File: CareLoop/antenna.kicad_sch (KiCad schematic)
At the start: 5 parts, among them J1 Conn_Coaxial_Small

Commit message: updated antenna version
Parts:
- removed C30: C_Small, Capacitor_SMD:C_0603_1608Metric_Pad1.08x0.95mm_HandSolder, symbol Device:C_Small
- added L3: L_Small, symbol Device:L_Small
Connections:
- net GND: now also L3.2; no longer C29.2
- net at C20.2, C29.1: now also L3.1; no longer AE1.1 (FEED)
- new net: AE1.1 (FEED), C29.2
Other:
- moved on the sheet: C20

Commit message: updated antenna version
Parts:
- removed C29: C_Small, Capacitor_SMD:C_0603_1608Metric_Pad1.08x0.95mm_HandSolder, symbol Device:C_Small
- added L4: L_Small, symbol Device:L_Small
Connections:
- net at AE1.1 (FEED): now also L4.2
- net at C20.2, L3.1: now also L4.1
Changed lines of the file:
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@@
+	(symbol
+		(lib_id "Device:L_Small")
+		(at 124.46 93.98 90)
+		(unit 1)
+		(exclude_from_sim no)
+		(in_bom yes)
+		(on_board yes)
+		(dnp no)
+		(fields_autoplaced yes)
+		(property "Reference" "L4"
+			(at 124.46 88.9 90)
+			(effects
+				(font
+					(size 1.27 1.27)
+				)
+			)
+		)
+		(property "Value" "L_Small"
+			(at 124.46 91.44 90)
+			(effects
+				(font
+					(size 1.27 1.27)
+				)
+			)
+		)
+		(property "Footprint" ""
+			(at 124.46 93.98 0)
+			(effects
+				(font
+					(size 1.27 1.27)
+				)
+				(hide yes)
+			)
+		)
+		(property "Datasheet" "~"
+			(at 124.46 93.98 0)
+			(effects
+				(font
+					(size 1.27 1.27)
+				)
+				(hide yes)
+			)
+		)
+		(property "Description" "Inductor, small symbol"
+			(at 124.46 93.98 0)
+			(effects
+				(font
+					(size 1.27 1.27)
+				)
+				(hide yes)
+			)
+		)
+		(pin "1"
+		)
+		(pin "2"
+		)
+		(instances
+			(project "CareLoop_PCB"
+				(path "/1249f778-de2d-49b4-b768-08b76b87278f/6a4240b2-fe07-4b72-99e3-52c15e65d120"
+					(reference "L4")
+					(unit 1)
+				)
+			)
+		)
+	)
 	(symbol
 		(lib_id "Device:L_Small")
@@
 					(unit 1)
 				)
-			)
-		)
-	)
-	(symbol
-		(lib_id "Device:C_Small")
-		(at 124.46 93.98 90)
-		(unit 1)
-		(exclude_from_sim no)
-		(in_bom yes)
-		(on_board yes)
-		(dnp no)
-		(fields_autoplaced yes)
-		(property "Reference" "C29"
-			(at 124.4663 87.63 90)
-			(effects
-				(font
-					(size 1.27 1.27)
-				)
-			)
-		)
-		(property "Value" "C_Small"
-			(at 124.4663 90.17 90)
-			(effects
-				(font
-					(size 1.27 1.27)
-				)
-			)
-		)
-		(property "Footprint" "Capacitor_SMD:C_0603_1608Metric_Pad1.08x0.95mm_HandSolder"
-			(at 124.46 93.98 0)
-			(effects
-				(font
-					(size 1.27 1.27)
-				)
-				(hide yes)
-			)
-		)
-		(property "Datasheet" "~"
-			(at 124.46 93.98 0)
-			(effects
-				(font
-					(size 1.27 1.27)
-				)
-				(hide yes)
-			)
-		)
-		(property "Description" "Unpolarized capacitor, small symbol"
-			(at 124.46 93.98 0)
-			(effects
-				(font
-					(size 1.27 1.27)
-				)
-				(hide yes)
-			)
-		)
-		(pin "2"
-		)
-		(pin "1"
-		)
-		(instances
-			(project "CareLoop_PCB"
-				(path "/1249f778-de2d-49b4-b768-08b76b87278f/6a4240b2-fe07-4b72-99e3-52c15e65d120"
-					(reference "C29")
-					(unit 1)
-				)

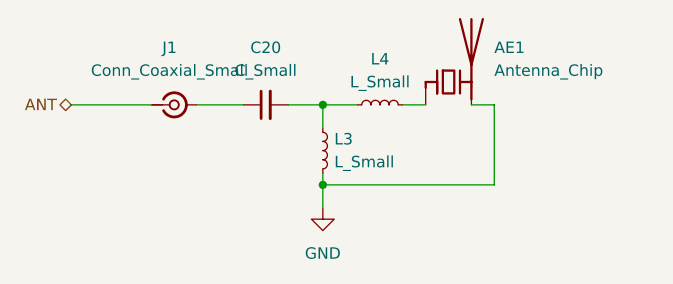
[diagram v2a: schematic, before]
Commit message: WP: Placement PCB Parts done
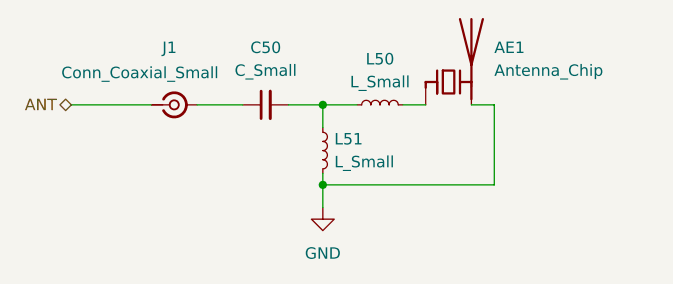
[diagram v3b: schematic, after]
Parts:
- AE1: footprint (none) -> RF_Antenna:Johanson_2450AT18x100
- C50: renamed from C20; footprint Capacitor_SMD:C_0603_1608Metric_Pad1.08x0.95mm_HandSolder -> Capacitor_SMD:C_0402_1005Metric_Pad0.74x0.62mm_HandSolder
- J1: footprint (none) -> Connector_Coaxial:U.FL_Molex_MCRF_73412-0110_Vertical
- L50: renamed from L4; footprint (none) -> Inductor_SMD:L_0402_1005Metric_Pad0.77x0.64mm_HandSolder
- L51: renamed from L3; footprint (none) -> Inductor_SMD:L_0402_1005Metric_Pad0.77x0.64mm_HandSolder
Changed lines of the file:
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@@
 			)
 		)
-		(property "Footprint" ""
+		(property "Footprint" "RF_Antenna:Johanson_2450AT18x100"
 			(at 129.54 86.995 0)
 			(effects
@@
 		(dnp no)
 		(fields_autoplaced yes)
-		(property "Reference" "L4"
+		(property "Reference" "L50"
 			(at 124.46 88.9 90)
 			(effects
@@
 			)
 		)
-		(property "Footprint" ""
+		(property "Footprint" "Inductor_SMD:L_0402_1005Metric_Pad0.77x0.64mm_HandSolder"
 			(at 124.46 93.98 0)
 			(effects
@@
 			(project "CareLoop_PCB"
 				(path "/1249f778-de2d-49b4-b768-08b76b87278f/6a4240b2-fe07-4b72-99e3-52c15e65d120"
-					(reference "L4")
+					(reference "L50")
 					(unit 1)
 				)
@@
 		(dnp no)
 		(fields_autoplaced yes)
-		(property "Reference" "L3"
+		(property "Reference" "L51"
 			(at 119.38 97.7899 0)
 			(effects
@@
 			)
 		)
-		(property "Footprint" ""
+		(property "Footprint" "Inductor_SMD:L_0402_1005Metric_Pad0.77x0.64mm_HandSolder"
 			(at 118.11 99.06 0)
 			(effects
@@
 			(project ""
 				(path "/1249f778-de2d-49b4-b768-08b76b87278f/6a4240b2-fe07-4b72-99e3-52c15e65d120"
-					(reference "L3")
+					(reference "L51")
 					(unit 1)
 				)
@@
 		(on_board yes)
 		(dnp no)
-		(fields_autoplaced yes)
 		(property "Reference" "J1"
 			(at 101.0804 87.63 0)
@@
 		)
 		(property "Value" "Conn_Coaxial_Small"
-			(at 101.0804 90.17 0)
-			(effects
-				(font
-					(size 1.27 1.27)
-				)
-			)
-		)
-		(property "Footprint" ""
+			(at 97.79 90.424 0)
+			(effects
+				(font
+					(size 1.27 1.27)
+				)
+			)
+		)
+		(property "Footprint" "Connector_Coaxial:U.FL_Molex_MCRF_73412-0110_Vertical"
 			(at 101.6 93.98 0)
 			(effects
@@
 		(dnp no)
 		(fields_autoplaced yes)
-		(property "Reference" "C20"
+		(property "Reference" "C50"
 			(at 111.7663 87.63 90)
 			(effects
@@
 			)
 		)
-		(property "Footprint" "Capacitor_SMD:C_0603_1608Metric_Pad1.08x0.95mm_HandSolder"
+		(property "Footprint" "Capacitor_SMD:C_0402_1005Metric_Pad0.74x0.62mm_HandSolder"
 			(at 111.76 93.98 0)
 			(effects
@@
 			(project ""
 				(path "/1249f778-de2d-49b4-b768-08b76b87278f/6a4240b2-fe07-4b72-99e3-52c15e65d120"
-					(reference "C20")
-					(unit 1)
-				)
+					(reference "C50")
+					(unit 1)
+				)

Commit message: update routing
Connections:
- net GND: no longer AE1.2 (PCB_Trace)
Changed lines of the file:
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@@
 		(color 0 0 0 0)
-	)
-	(junction
-		(at 118.11 102.87)
-		(diameter 0)
-		(color 0 0 0 0)
-	)
-	(wire
-		(pts
-			(xy 118.11 102.87) (xy 137.16 102.87)
-		)
-		(stroke
-			(width 0)
-			(type default)
-		)
 	)
 	(wire
@@
 	(wire
 		(pts
-			(xy 118.11 101.6) (xy 118.11 102.87)
+			(xy 118.11 101.6) (xy 118.11 105.41)
 		)
 		(stroke
@@
 		(pts
 			(xy 90.17 93.98) (xy 99.06 93.98)
-		)
-		(stroke
-			(width 0)
-			(type default)
-		)
-	)
-	(wire
-		(pts
-			(xy 118.11 102.87) (xy 118.11 105.41)
 		)
 		(stroke
@@
 		)
 		(stroke
-			(width 0)
-			(type default)
-		)
-	)
-	(wire
-		(pts
-			(xy 134.62 93.98) (xy 137.16 93.98)
-		)
-		(stroke
-			(width 0)
-			(type default)
-		)
-	)
-	(wire
-		(pts
-			(xy 137.16 93.98) (xy 137.16 102.87)
-		)
-		(stroke

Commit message: update PCB
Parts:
- removed J1: Conn_Coaxial_Small, Connector_Coaxial:U.FL_Molex_MCRF_73412-0110_Vertical, symbol Connector:Conn_Coaxial_Small
- AE1: JLCPCB Part#(optional) (none) -> C2917717
- C50, L50, L51: now not fitted
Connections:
- net ANT: now also C50.1
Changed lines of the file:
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@@
 	(wire
 		(pts
-			(xy 90.17 93.98) (xy 99.06 93.98)
-		)
-		(stroke
-			(width 0)
-			(type default)
-		)
-	)
-	(wire
-		(pts
-			(xy 104.14 93.98) (xy 109.22 93.98)
+			(xy 90.17 93.98) (xy 109.22 93.98)
 		)
 		(stroke
@@
 			)
 		)
+		(property "JLCPCB Part#(optional)" "C2917717"
+			(at 132.08 91.44 0)
+			(effects
+				(font
+					(size 1.27 1.27)
+				)
+				(hide yes)
+			)
+		)
 		(pin "1"
 		)
@@
 		(in_bom yes)
 		(on_board yes)
-		(dnp no)
+		(dnp yes)
 		(fields_autoplaced yes)
 		(property "Reference" "L50"
@@
 		(property "Description" "Inductor, small symbol"
 			(at 124.46 93.98 0)
+			(effects
+				(font
+					(size 1.27 1.27)
+				)
+				(hide yes)
+			)
+		)
+		(property "JLCPCB Part#(optional)" ""
+			(at 124.46 93.98 90)
 			(effects
 				(font
@@
 		(in_bom yes)
 		(on_board yes)
-		(dnp no)
+		(dnp yes)
 		(fields_autoplaced yes)
 		(property "Reference" "L51"
@@
 		)
 		(property "Description" "Inductor, small symbol"
+			(at 118.11 99.06 0)
+			(effects
+				(font
+					(size 1.27 1.27)
+				)
+				(hide yes)
+			)
+		)
+		(property "JLCPCB Part#(optional)" ""
 			(at 118.11 99.06 0)
 			(effects
@@
 	)
 	(symbol
-		(lib_id "Connector:Conn_Coaxial_Small")
-		(at 101.6 93.98 0)
-		(unit 1)
-		(exclude_from_sim no)
-		(in_bom yes)
-		(on_board yes)
-		(dnp no)
-		(property "Reference" "J1"
-			(at 101.0804 87.63 0)
-			(effects
-				(font
-					(size 1.27 1.27)
-				)
-			)
-		)
-		(property "Value" "Conn_Coaxial_Small"
-			(at 97.79 90.424 0)
-			(effects
-				(font
-					(size 1.27 1.27)
-				)
-			)
-		)
-		(property "Footprint" "Connector_Coaxial:U.FL_Molex_MCRF_73412-0110_Vertical"
-			(at 101.6 93.98 0)
-			(effects
-				(font
-					(size 1.27 1.27)
-				)
-				(hide yes)
-			)
-		)
-		(property "Datasheet" "~"
-			(at 101.6 93.98 0)
-			(effects
-				(font
-					(size 1.27 1.27)
-				)
-				(hide yes)
-			)
-		)
-		(property "Description" "small coaxial connector (BNC, SMA, SMB, SMC, Cinch/RCA, LEMO, ...)"
-			(at 101.6 93.98 0)
-			(effects
-				(font
-					(size 1.27 1.27)
-				)
-				(hide yes)
-			)
-		)
-		(pin "2"
-		)
-		(pin "1"
-		)
-		(instances
-			(project ""
-				(path "/1249f778-de2d-49b4-b768-08b76b87278f/6a4240b2-fe07-4b72-99e3-52c15e65d120"
-					(reference "J1")
-					(unit 1)
-				)
-			)
-		)
-	)
-	(symbol
 		(lib_id "Device:C_Small")
 		(at 111.76 93.98 90)
@@
 		(in_bom yes)
 		(on_board yes)
-		(dnp no)
+		(dnp yes)
 		(fields_autoplaced yes)
 		(property "Reference" "C50"
@@
 			(effects
 				(font
+					(size 1.27 1.27)
+				)
+				(hide yes)
+			)
+		)
+		(property "JLCPCB Part#(optional)" ""
+			(at 111.76 93.98 90)
+			(effects
+				(font
